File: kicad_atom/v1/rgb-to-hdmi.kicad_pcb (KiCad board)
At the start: 2 copper layers, 121.9 x 81.3 mm, 53 parts, among them J1 Conn_02x05_Odd_Even, J2 Conn_01x20, J3 Conn_01x20, J4 Conn_01x03, J5 Conn_02x20_Odd_Even, SW1 SW_Push_Dual, SW2 SW_Push_Dual, SW3 SW_Push_Dual, U1 74LVC1G66, U2 LM319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

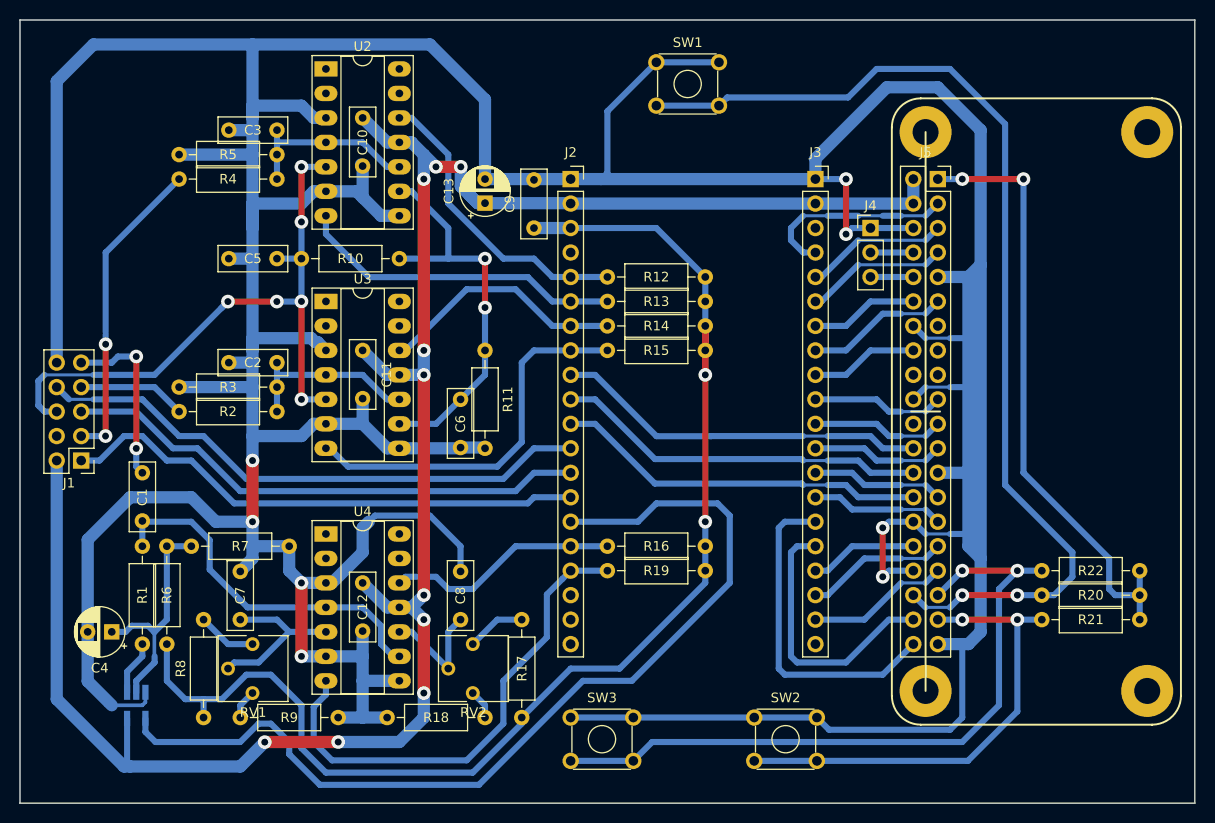
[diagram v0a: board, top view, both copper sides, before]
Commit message: Atom PCB: Prototype (just about complete)
Change-Id: Iee45754a64bc2e643c024d613505a408e311c64b
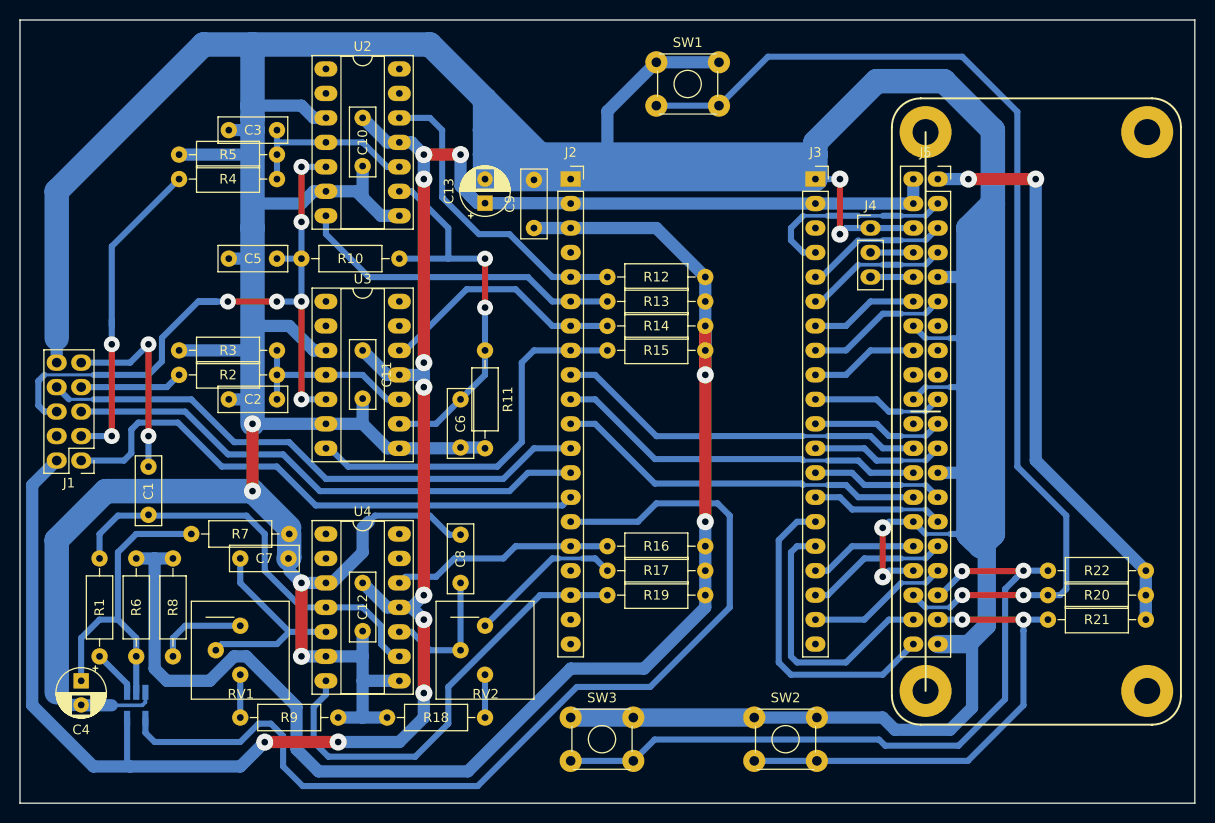
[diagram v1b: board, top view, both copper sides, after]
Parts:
- C1, C10, C11, C12, C2, C3, C5, C6, C7, C8, C9: footprint Capacitor_THT:C_Rect_L7.0mm_W2.5mm_P5.00mm -> local:C_Rect_L7.0mm_W2.5mm_P5.00mm
- C13, C4: footprint Capacitor_THT:CP_Radial_D5.0mm_P2.50mm -> local:CP_Radial_D5.0mm_P2.50mm
- J1: footprint Connector_PinHeader_2.54mm:PinHeader_2x05_P2.54mm_Vertical -> local:PinHeader_2x05_P2.54mm_Vertical
- J2, J3: footprint Connector_PinSocket_2.54mm:PinSocket_1x20_P2.54mm_Vertical -> local:PinSocket_1x20_P2.54mm_Vertical
- J4: footprint Connector_PinHeader_2.54mm:PinHeader_1x03_P2.54mm_Vertical -> local:PinHeader_1x03_P2.54mm_Vertical
- J5: footprint Connector_PinSocket_2.54mm:PinSocket_2x20_P2.54mm_Vertical -> local:PinSocket_2x20_P2.54mm_Vertical
- R1, R10, R11, R12, R13, R14, R15, R16, R17, R18, R19, R2, R20, R21, R22, R3, R4, R5, R6, R7, R8, R9: footprint Resistor_THT:R_Axial_DIN0207_L6.3mm_D2.5mm_P10.16mm_Horizontal -> local:R_Axial_DIN0207_L6.3mm_D2.5mm_P10.16mm_Horizontal
- RV1, RV2: footprint Potentiometer_THT:Potentiometer_Vishay_T73YP_Vertical -> local:Potentiometer_Vishay_T73YP_Vertical
- SW1, SW2, SW3: footprint Button_Switch_THT:SW_TH_Tactile_Omron_B3F-10xx -> local:SW_TH_Tactile_Omron_B3F-10xx
- U2, U3, U4: footprint Package_DIP:DIP-14_W7.62mm_Socket_LongPads -> local:DIP-14_W7.62mm_Socket_LongPads
- moved R17 24.4 mm to (191.8, 129.5), turned to 180 degrees
- moved R8 16.8 mm to (136.5, 128.3), turned to 270 degrees
- moved R6 9.44 mm to (132.7, 128.3), turned to 270 degrees
- moved C7 6.35 mm to (143.5, 128.3), turned to 0 degrees
- moved C4 5.99 mm to (127.0, 141.0), turned to 270 degrees
- moved R1 4.62 mm to (128.9, 128.3)
- moved C2 3.81 mm to (147.3, 111.8)
- moved C8 3.81 mm to (166.4, 130.8)
- moved R2 3.81 mm to (137.2, 109.2)
- moved R3 3.81 mm to (147.3, 106.7)
- moved R19 2.54 mm to (191.8, 132.1)
- moved RV1 2.29 mm to (143.5, 135.3)
- moved RV2 2.29 mm to (168.9, 135.3)
- moved R7 1.27 mm to (138.4, 125.7)
- moved C1 0.90 mm to (134.0, 118.7)
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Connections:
- J2 pad 17: SYNC -> (no net)
- J2 pad 18: (no net) -> SYNC
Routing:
- net GND: track 613.2 -> 695.7 mm
- net +3V3: track 145.6 -> 157.3 mm
- net Net-(R17-Pad2): track 6.13 -> 17.4 mm
- net Net-(C4-Pad1): track 24.1 -> 33.5 mm
- net VCC: track 212.2 -> 218.1 mm
- net Net-(C1-Pad2): track 38.8 -> 44.6 mm
- net SYNC: track 51.5 -> 47.2 mm
- net Net-(C7-Pad1): track 17.3 -> 21.3 mm
- net Net-(R8-Pad2): track 6.13 -> 9.42 mm
- net +3.3VP: track 63.6 -> 60.6 mm
- net CSS: track 55.0 -> 57.8 mm
- net CLAMP: track 100.1 -> 102.9 mm
- net gpio16: track 108.4 -> 110.8 mm
- net /CB: track 68.2 -> 70.5 mm
- net Net-(C1-Pad1): track 18.3 -> 20.5 mm
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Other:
- net class Default: via_dia 1.4224 -> 1.651; via_drill 0.7112 -> 0.6858
- net class Power: via_dia 1.4224 -> 1.778; via_drill 0.7112 -> 0.6858

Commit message: Atom PCB: Prototype (improved ground routing)
Change-Id: Ib0ffeedc2e691b3e808bfd0fe7fde48a0fe1ef16
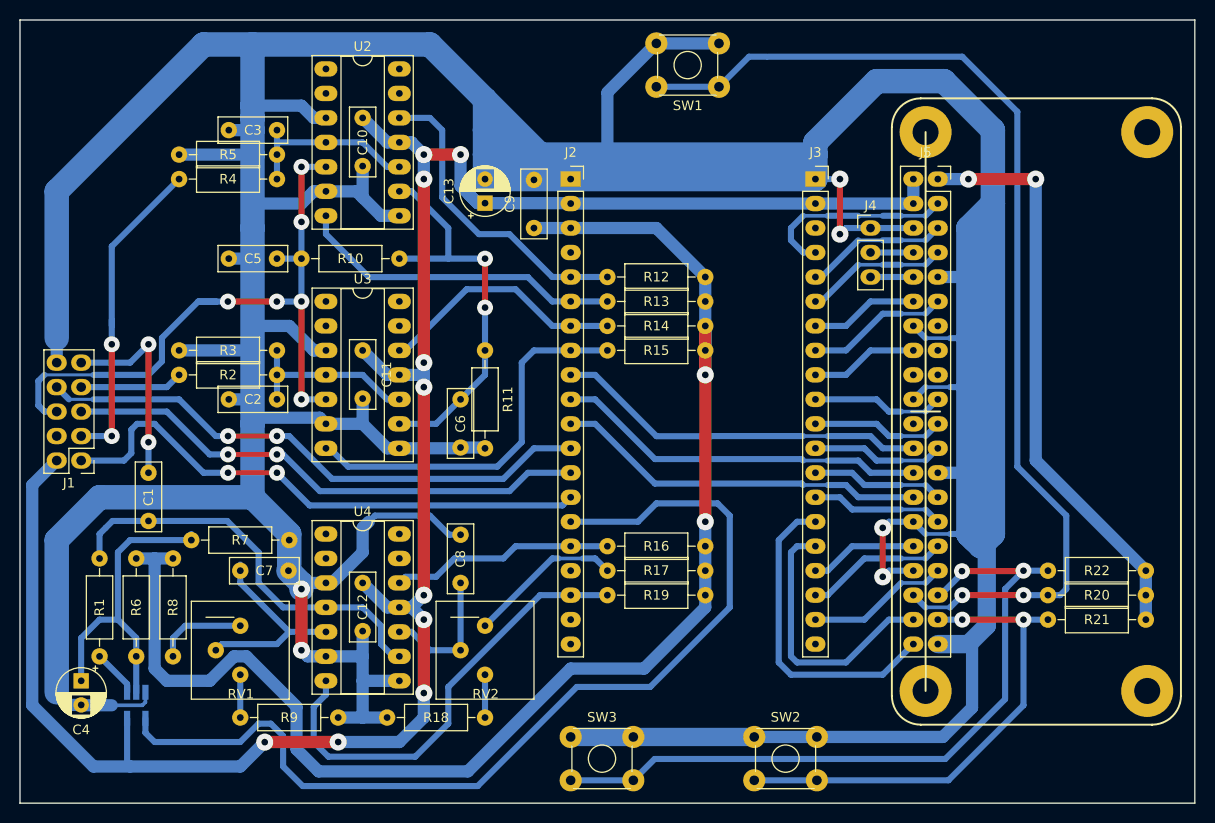
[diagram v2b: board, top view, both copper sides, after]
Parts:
- moved SW2 2.01 mm to (196.8, 146.8)
- moved SW3 2.01 mm to (177.8, 146.8)
- moved SW1 1.96 mm to (186.7, 74.8)
- moved C7 1.27 mm to (143.5, 129.5)
- moved C1 0.63 mm to (134.0, 119.4)
- moved R7 0.63 mm to (138.4, 126.4)
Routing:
- net GND: track 695.7 -> 699.2 mm, vias 8 -> 6
- net gpio16: track 110.8 -> 109.8 mm
- net gpio26: track 50.7 -> 51.5 mm
- net Net-(C1-Pad2): track 44.6 -> 43.8 mm
- net CSS: track 57.8 -> 57.7 mm, vias 0 -> 2
- net HS_N: vias 0 -> 2
- net FS_N: vias 0 -> 2
